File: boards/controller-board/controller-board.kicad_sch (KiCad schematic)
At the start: 71 parts, among them J1 Conn_01x02, J2 Conn_01x02, J3 Conn_01x02, J4 Conn_01x02, J5 Conn_01x03, J6 Phoenix 1995499, Q1 PMV45EN, Q2 Goford_G11S_20V_11A, SW1 EG1271, U1 LTC3624, U2 ADS1015IRUGR, U3 ADS1015IRUGR, U4 RPi_Pico, U5 MCP4728

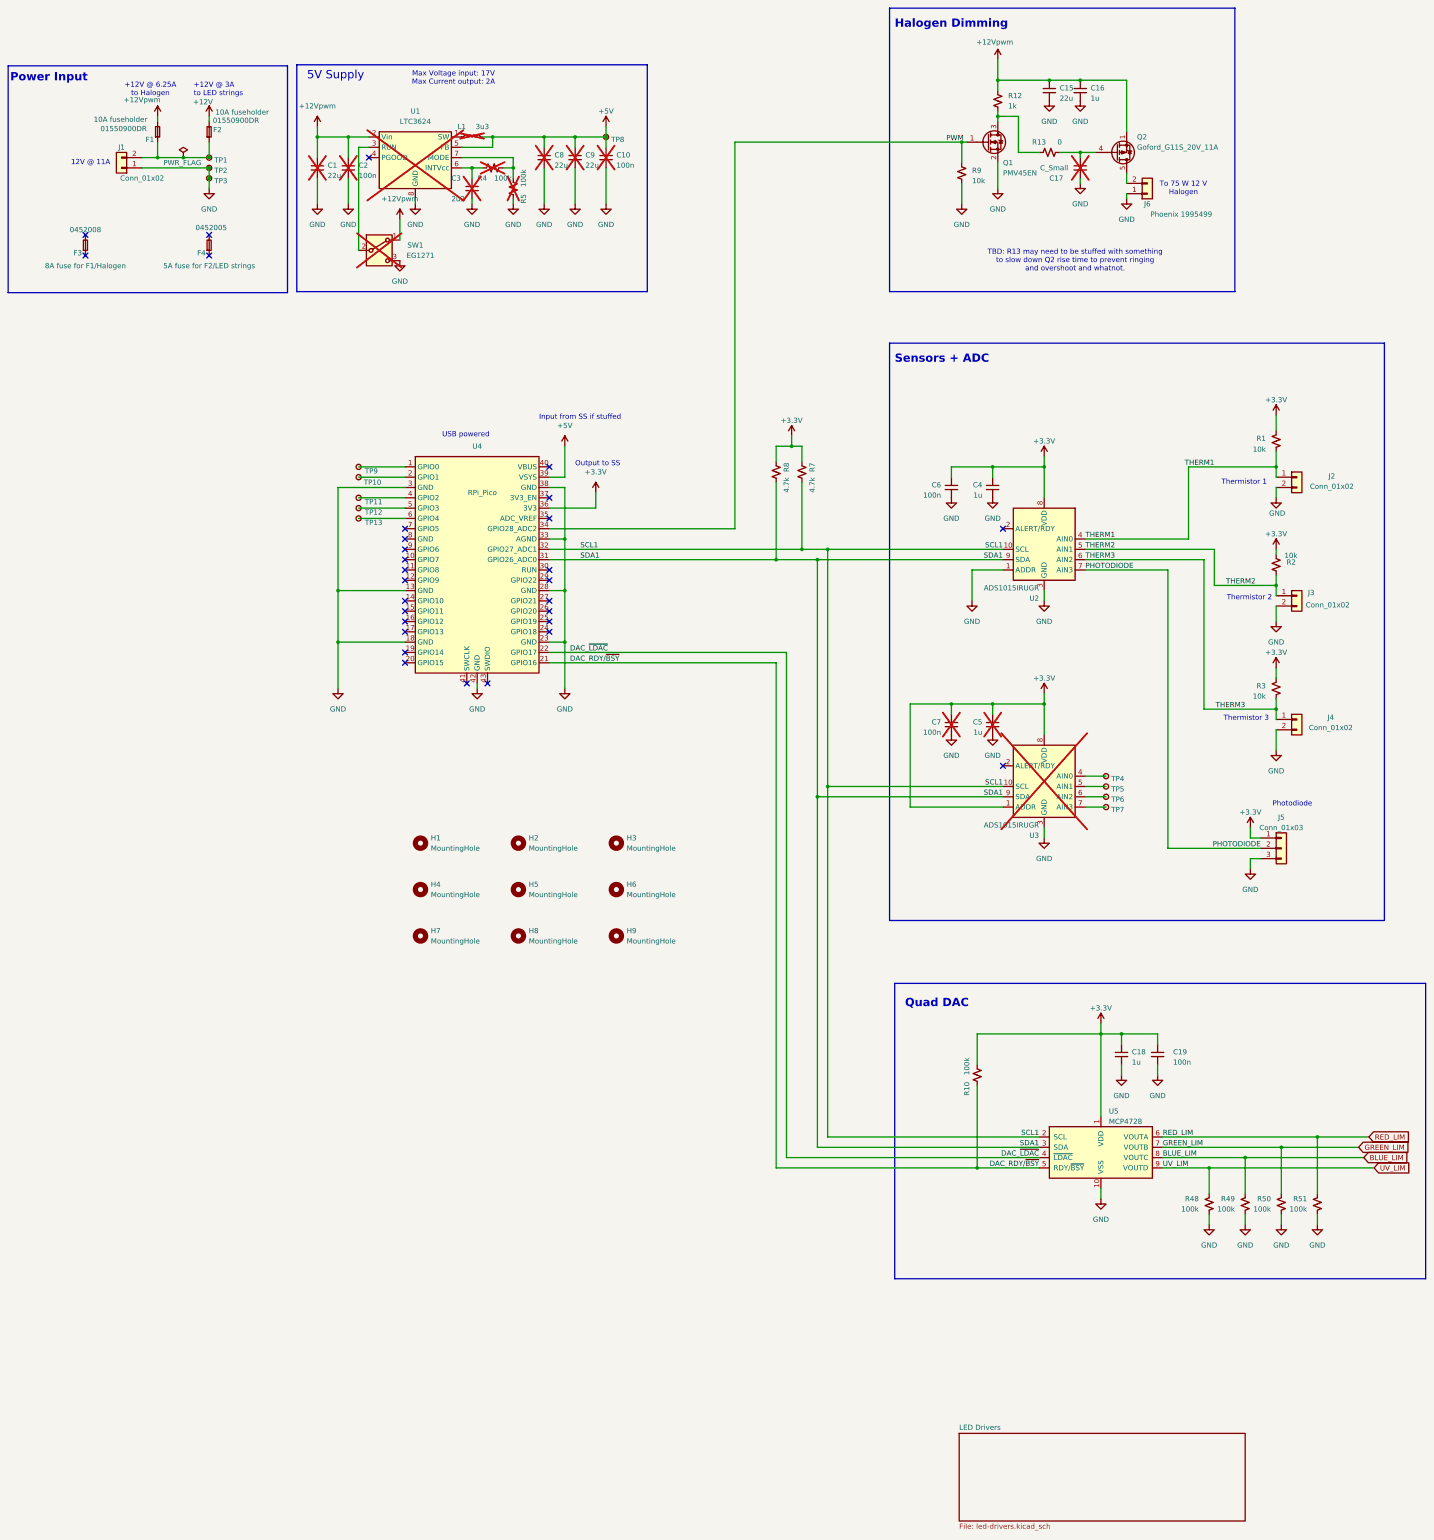
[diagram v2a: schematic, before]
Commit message: Move schematics off of root page onto its own sheet. Rename sheets to be oresat standard naming convention. Clean up 0603 and 0402 footprints to be oresat passives. Sort BOM by footprint. Clean up silkscreen. Finally, clean up solar sim repository, removing old capstone software files (should be in software repo).
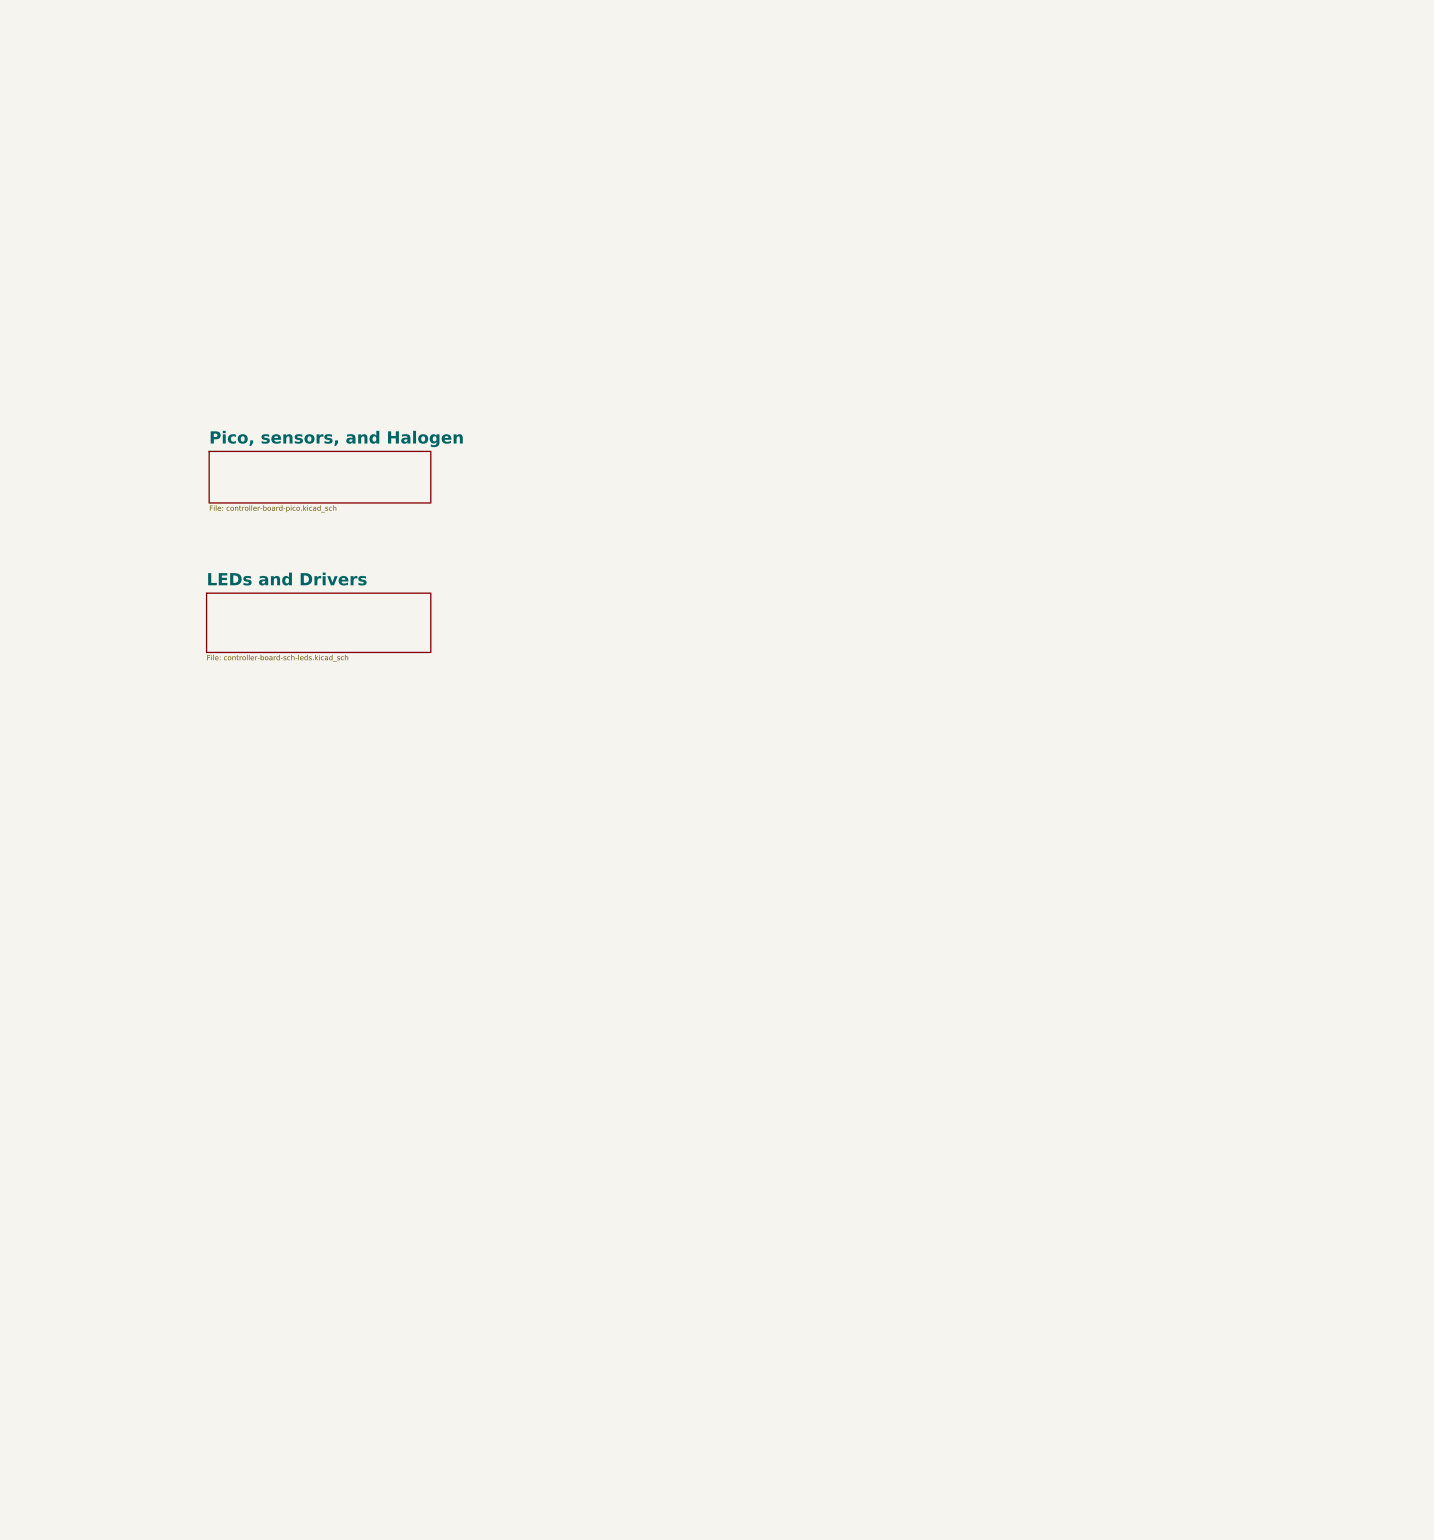
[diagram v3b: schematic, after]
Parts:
- removed C1, C15, C8, C9: 22u, Capacitor_SMD:C_1210_3225Metric, symbol Device:C_Small
- removed C10, C19, C2, C6, C7: 100n, Capacitor_SMD:C_0603_1608Metric, symbol Device:C_Small
- removed C16, C18, C4, C5: 1u, Capacitor_SMD:C_0603_1608Metric, symbol Device:C_Small
- removed C17: C_Small, Capacitor_SMD:C_0603_1608Metric, symbol Device:C_Small
- removed C3: 2u2, Capacitor_SMD:C_0603_1608Metric, symbol Device:C_Small
- removed F1, F2: 01550900DR, Fuse:Fuseholder_Littelfuse_Nano2_154x, symbol Device:Fuse_Small
- removed F3: 0452008, symbol Device:Fuse_Small
- removed F4: 0452005, Fuse:Fuseholder_Littelfuse_Nano2_154x, symbol Device:Fuse_Small
- removed H1, H2, H3, H4, H5, H6, H7, H8, H9: MountingHole, oresat-misc:MountingHole_3.2mm_M3, symbol Mechanical:MountingHole
- removed J1: Conn_01x02, TerminalBlock_Phoenix:TerminalBlock_Phoenix_PT-1,5-2-5.0-H_1x02_P5.00mm_Horizontal, symbol Connector_Generic:Conn_01x02
- removed J2, J3, J4: Conn_01x02, Connector_PinHeader_2.54mm:PinHeader_1x02_P2.54mm_Vertical, symbol Connector_Generic:Conn_01x02
- removed J5: Conn_01x03, Connector_PinHeader_2.54mm:PinHeader_1x03_P2.54mm_Vertical, symbol Connector_Generic:Conn_01x03
- removed J6: Phoenix 1995499, TerminalBlock_Phoenix:TerminalBlock_Phoenix_PT-1,5-2-5.0-H_1x02_P5.00mm_Horizontal, symbol Connector_Generic:Conn_01x02
- removed L1: 3u3, oresat-passives:L_ECS-MPI4040, symbol Device:L_Small
- removed Q1: PMV45EN, Package_TO_SOT_SMD:SOT-23-3, symbol Device:Q_NMOS_GSD
- removed Q2: Goford_G11S_20V_11A, Package_SO:SOP-8_3.9x4.9mm_P1.27mm, symbol oresat-transistors:Goford_G11S_20V_11A
- removed R1, R2, R3, R9: 10k, Resistor_SMD:R_0603_1608Metric, symbol Device:R_Small_US
- removed R10, R4, R5: 100k, Resistor_SMD:R_0603_1608Metric, symbol Device:R_Small_US
- removed R12: 1k, Resistor_SMD:R_0603_1608Metric, symbol Device:R_Small_US
- removed R13: 0, Resistor_SMD:R_0603_1608Metric, symbol Device:R_Small_US
- removed R48, R49, R50, R51: 100k, oresat-passives:0603-C, symbol Device:R_Small_US
- removed R7, R8: 4.7k, Resistor_SMD:R_0603_1608Metric, symbol Device:R_Small_US
- removed SW1: EG1271, Button_Switch_THT:SW_E-Switch_EG1271_SPDT, symbol Switch:SW_SPDT
- removed TP1, TP10, TP11, TP12, TP13, TP2, TP3, TP4, TP5, TP6, TP7, TP8, TP9: TestPoint-MinTH, oresat-misc:TestPoint-MinTH, symbol oresat-misc:TestPoint-MinTH
- removed U1: LTC3624, oresat-ics:DFN-8-1EP_3x3mm_P0.5mm_EP1.65x2.38mm_ThermalVias0.3mm, symbol oresat-ics:LTC3624
- removed U2, U3: ADS1015IRUGR, Package_DFN_QFN:Texas_R-PUQFN-N10, symbol Analog_ADC:ADS1015IDGS
- removed U4: RPi_Pico, oresat-misc:RPi_Pico_TH, symbol oresat-misc:RPi_Pico
- removed U5: MCP4728, Package_SO:MSOP-10_3x3mm_P0.5mm, symbol Analog_DAC:MCP4728
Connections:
- no-connect marks 30 -> 0
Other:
- sheet LED Drivers renamed LEDs and Drivers
- added sheet Pico, sensors, and Halogen (controller-board-pico.kicad_sch)
- sheet LEDs and Drivers: file led-drivers.kicad_sch -> controller-board-sch-leds.kicad_sch
- note removed: "+12V @ 3A to LED strings"
- note removed: "+12V @ 6.25A to Halogen"
- note removed: "12V @ 11A"
- note removed: "5V Supply"
- note removed: "Halogen Dimming"
- note removed: "Input from SS if stuffed"
- note removed: "Max Voltage input: 17V Max Current output: 2A"
- note removed: "Output to SS"
- note removed: "Photodiode"
- note removed: "Power Input"
- note removed: "Quad DAC"
- note removed: "Sensors + ADC"
- note removed: "TBD: R13 may need to be stuffed with something to slow down Q2 rise time to prevent ringing and overshoot and whatnot."
- note removed: "Thermistor 1"
- note removed: "Thermistor 2"
- note removed: "Thermistor 3"
- note removed: "To 75 W 12 V Halogen"
- note removed: "USB powered"
